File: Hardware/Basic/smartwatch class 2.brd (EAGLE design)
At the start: 38 x 38 mm, 52 parts, among them SW3 SWITCH.MOM, SW4 SWITCH.MOM, SW5 SWITCH.MOM, U1 NRF52832_MODULE_MDBT42, U4 PCF8523

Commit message: finished class 2 video
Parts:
- moved LDO2 21.6 mm to (2.64, 26.0)
- moved R12 20.8 mm to (2.11, 20.6)
- moved R11 20.7 mm to (2.57, 17.6)
- moved C20 15.5 mm to (30.4, 17.7)
- moved J2 15.2 mm to (2.18, 36.1)
- moved R14 14.4 mm to (36.2, 15.6)
- moved R13 14.2 mm to (32.4, 14.8)
- moved CHRG2 8.52 mm to (11.0, 8.79)
- moved C12 5.68 mm to (21.2, 9.42)
- moved R15 5.68 mm to (19.1, 9.37)
- moved SW3 5.08 mm to (11.4, 3.81)
- moved D5 5.08 mm to (27.1, 7.92)
- moved C21 3.81 mm to (15.5, 8.86)
- moved SW4 3.81 mm to (21.6, 3.81)
- moved C11 2.84 mm to (23.5, 9.42)
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
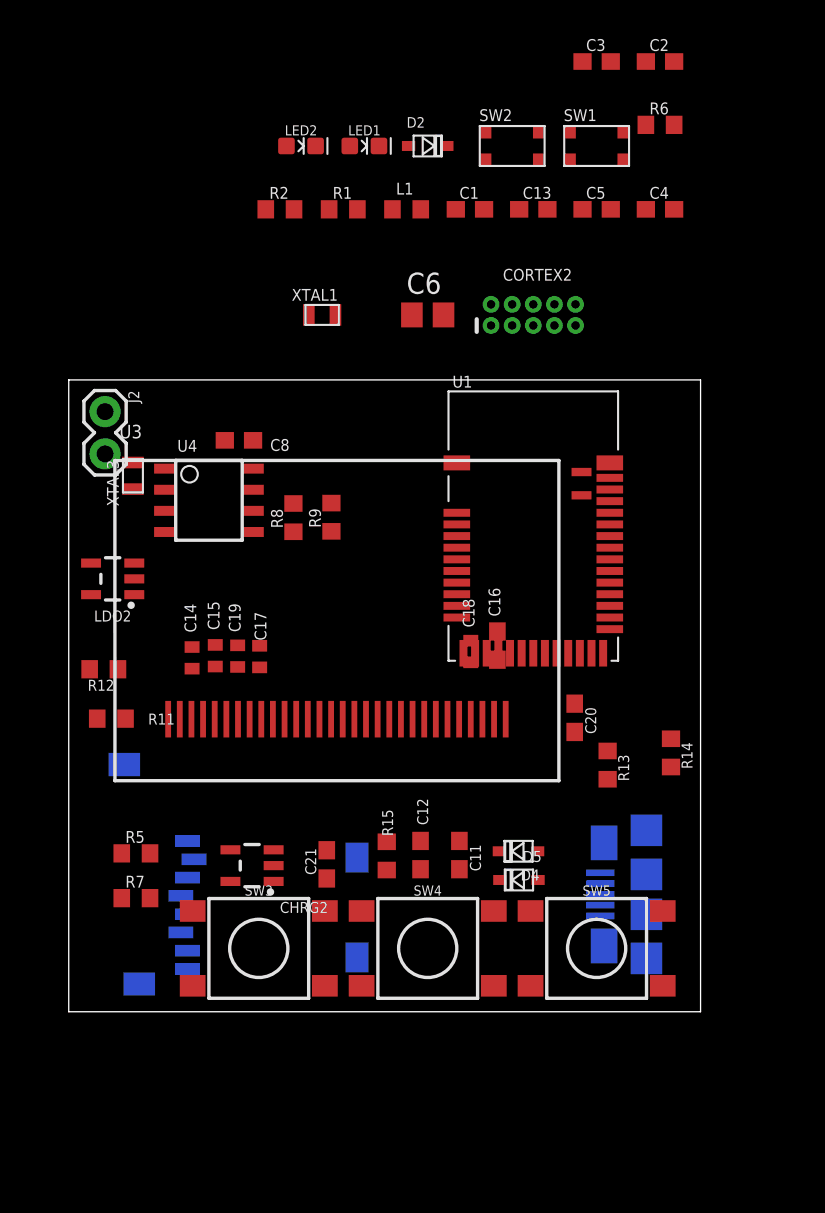
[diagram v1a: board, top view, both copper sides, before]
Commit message: deleted the second board and partially wired the board
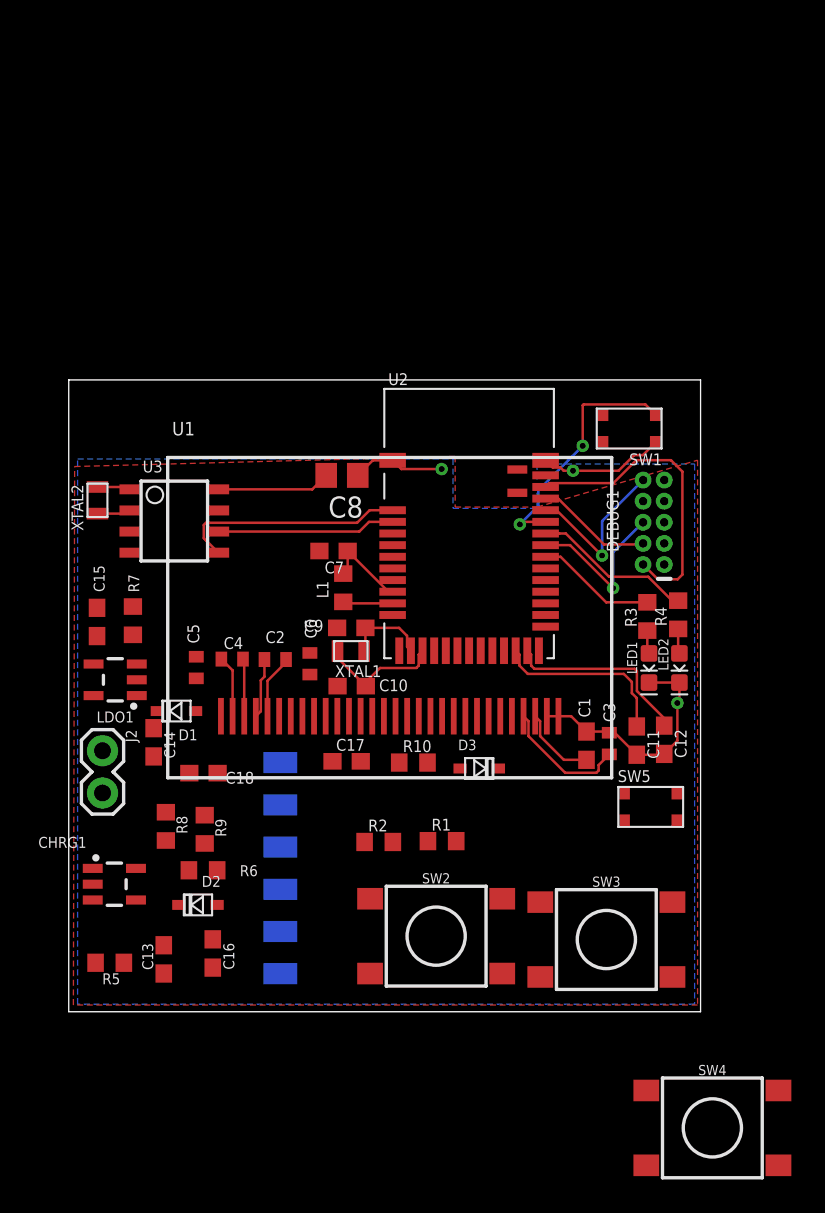
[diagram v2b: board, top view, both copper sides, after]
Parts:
- removed C19: 2.2uF, LinnesLab-Passives:C0402
- removed C20, C21: 4.7u, LinnesLab-Passives:C0603
- removed CHRG2: MCP73831, LinnesLab-Power:SOT23-5
- removed CORTEX2: CORTEX_DEBUG_PTH, LinnesLab-Connectors:2X5-PTH-1.27MM
- removed D4, D5: (no value), LinnesLab-DiscreteSemi:USC
- removed LDO2: MIC5504, LinnesLab-Power:SOT23-5
- removed R11: (no value), LinnesLab-Passives:R0603
- removed R12, R13, R14, R15: 100k, LinnesLab-Passives:R0603
- removed SD2: (no value), LinnesLab-Connectors:MICROSD
- removed U4: PCF8523, LinnesLab-Clocks:SO8
- removed USB2: USB.MICRO-BIGGERPADS, LinnesLab-Connectors:USB-MICRO-01.BIGGERPADS
- removed XTAL3: 32.7680kHz, LinnesLab-Clocks:2-SMD.NOLEAD.2.0MMTO1.2MM
- added C10, C9: (no value), LinnesLab-Passives:C0603
- added C7: 1u, LinnesLab-Passives:C0603
- added CHRG1: MCP73831, LinnesLab-Power:SOT23-5
- added D1, D3: (no value), LinnesLab-DiscreteSemi:USC
- added DEBUG1: CORTEX_DEBUG_PTH, LinnesLab-Connectors:2X5-PTH-1.27MM
- added J1: FTDI_DEVICESMD, LinnesLab-Connectors:FTDI-SMD
- added LDO1: MIC5504, LinnesLab-Power:SOT23-5
- added R10: 10k, LinnesLab-Passives:R0603
- added R3, R4: 1k, LinnesLab-Passives:R0603
- added U2: NRF52832_MODULE_MDBT42, LinnesLab-Microcontrollers:BLE_MODULE_RAYTAC_MDBT42
- added XTAL2: 32.7680kHz, LinnesLab-Clocks:2-SMD.NOLEAD.2.0MMTO1.2MM
- C1: value 1u -> 10uF
- C11, C12: value 1u -> 300p
- C13: value 100n -> 4.7u
- C14, C15, C18: value 2.2uF -> 1u; device LinnesLab-Passives:C0402 -> LinnesLab-Passives:C0603
- C16: value 10uF -> 4.7u
- C17: value 2.2uF -> 100n; device LinnesLab-Passives:C0402 -> LinnesLab-Passives:C0603
- C2, C3: value (none) -> 2.2uF; device LinnesLab-Passives:C0603 -> LinnesLab-Passives:C0402
- C4, C5: value 300p -> 2.2uF; device LinnesLab-Passives:C0603 -> LinnesLab-Passives:C0402
- C6: value 10u -> 2.2uF; device LinnesLab-Passives:C0805 -> LinnesLab-Passives:C0402
- C8: value 1u -> 10u; device LinnesLab-Passives:C0603 -> LinnesLab-Passives:C0805
- R1: value 1k -> 10k
- R2: value 1k -> 390k
- R5, R8, R9: value 10k -> 100k
- R6: value 10k -> (none)
- R7: value 390k -> 100k
- SW2: value (none) -> SWITCH.MOM; device LinnesLab-Switches:BUTTON-GULLWING -> LinnesLab-Switches:TACTILE_SWITCH_SMD_6.2MM_TALL
- SW5: value SWITCH.MOM -> (none); device LinnesLab-Switches:TACTILE_SWITCH_SMD_6.2MM_TALL -> LinnesLab-Switches:BUTTON-GULLWING
- U1: value NRF52832_MODULE_MDBT42 -> (none); device LinnesLab-Microcontrollers:BLE_MODULE_RAYTAC_MDBT42 -> LinnesLab-Displays:UG-2864HSWEG01_0.96IN_NO-WRAPAROUND
- U3: value (none) -> PCF8523; device LinnesLab-Displays:UG-2864HSWEG01_0.96IN_NO-WRAPAROUND -> LinnesLab-Clocks:SO8
- moved R6 52.6 mm to (8.08, 8.51)
- moved C13 50.3 mm to (5.71, 3.15), turned to 90 degrees
- moved SW2 47.7 mm to (22.1, 4.55)
- moved D2 47.7 mm to (7.77, 6.43), turned to 180 degrees
- moved C2 42.8 mm to (12.4, 21.2), turned to 180 degrees
- moved C3 41.0 mm to (32.5, 16.1), turned to 270 degrees
- moved LED2 38.8 mm to (36.7, 20.7), turned to 270 degrees
- moved R2 38.5 mm to (18.6, 10.2)
- moved R1 38.5 mm to (22.5, 10.3)
- moved C4 37.3 mm to (9.83, 21.2), turned to 180 degrees
- moved C5 36.6 mm to (7.67, 20.7), turned to 270 degrees
- moved LED1 35.8 mm to (34.9, 20.7), turned to 270 degrees
- moved C1 33.0 mm to (31.1, 16.0), turned to 270 degrees
- moved C16 25.2 mm to (8.66, 3.51)
- moved L1 23.1 mm to (16.5, 25.5), turned to 90 degrees
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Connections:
- removed net BATT: R13.1, R14.2
- removed net CD1: SD2.CD1
- removed net CD2: SD2.CD2
- removed net CHRG.STAT: CHRG2.1, R12.1
- removed net CS.OLED: U3.13
- removed net DC.OLED: U3.15
- removed net RESET.OLED: U3.14
- removed net SD.CS: SD2.2
- removed net USB+: USB2.3
- removed net USB-: USB2.2
- new net A4/PPG: U2.5
- new net A5/TIA: U2.6
- new net A7.BATT: R8.1, R9.2
- new net A7/BATT: U2.8
- new net D11/SW1: SW2.A1, U2.25
- new net D15/SW2: SW3.A1, U2.29
- new net D16/CS.OLED: U1.13, U2.30
- new net D27/CHRG.STAT: CHRG1.1, R5.1
- new net D27/CHRG.STATUS: U2.4
- new net D3/RESET.OLED: U1.14, U2.16
- new net D30/LED.CTRL: U2.7
- new net D4/DC.OLED: U1.15, U2.17
- new net D5/CD1: U2.18
- new net D7/SD.CS: U2.20
- new net RXD.NRF: J1.TXO
- new net TXD.NRF: J1.RXI
- net 3.3V: now also C15.1, C18.1, C5.2, C8.2, D3.-, DEBUG1.1, LDO1.5, R10.2, R7.2, U1.6, U1.9, U2.11, U3.8; no longer C12.1, C17.2, C19.2, C8.1, CORTEX2.1, D2.-, LDO2.5, R15.2, R6.2, R8.2, R9.2, SD2.4, U1.11, U3.6, U3.9, U4.8
- net DFU: now also U2.34; no longer U1.34
- net DTR: now also C17.1, J1.DTR; no longer C13.1
- net FRST: now also U2.38; no longer U1.38
- net GND: now also C1.1, C10.2, C11.2, C13.1, C14.1, C15.2, C16.2, C18.2, C3.1, C5.1, C7.2, C8.1, C9.1, CHRG1.2, DEBUG1.3, DEBUG1.5, DEBUG1.7, DEBUG1.9, J1.CTS, J1.GND, LDO1.2, R1.1, R2.2, R6.1, R7.1, R9.1, SW2.B1, SW3.B1, SW5.3, U1.10, U1.29, U1.30, U1.8, U2.1, U2.12, U2.24, U2.39, U3.4; no longer C1.2, C11.1, C16.1, C17.1, C18.1, C19.1, C2.1, C20.2, C21.1, C3.2, C4.2, C5.2, C8.2, CHRG2.2, CORTEX2.3, CORTEX2.5, CORTEX2.7, CORTEX2.9, LDO2.2, R11.1, R14.1, R15.1, R5.1, R7.2, SD2.6, SD2.MT1, SD2.MT2, SW2.3, U1.24, U1.39, U3.1, U3.10, U3.12, U3.29, U3.30, U3.8, U4.4, USB2.5
- net LED1: now also R3.2, U2.31; no longer R1.2, U1.31
- net LED2: now also R4.2, U2.33; no longer R2.2, U1.33
- net MISO: now also U2.28; no longer SD2.7, U1.28
- net MOSI: now also U1.19, U2.27; no longer SD2.3, U1.27, U3.19
- net N$1: now also C9.2, U2.13; no longer C2.2, U1.13
- net N$10: now also C4.1, U1.3; no longer C14.1, U3.3
- net N$11: now also C2.2, U1.4; no longer C15.2, U3.4
- net N$12: now also C2.1, U1.5; no longer C15.1, U3.5
- net N$13: now also DEBUG1.8; no longer CORTEX2.8
- net N$14: now also C1.2, U1.28; no longer C16.2, U3.28
- net N$15: now also C3.2, U1.27; no longer C18.2, U3.27
- net N$17: now also CHRG1.5, R6.2; no longer CHRG2.5, R11.2
- net N$19: now also U3.2, XTAL2.P$1; no longer U4.2, XTAL3.P$1
- net N$2: now also C10.1, U2.14; no longer C3.1, U1.14
- net N$20: now also U3.1, XTAL2.P$2; no longer U4.1, XTAL3.P$2
- net N$3: now also U2.10; no longer U1.10
- net N$4: now also R1.2, U1.11; no longer R5.2, U3.11
- net N$5: now also R3.1; no longer R1.1
- net N$6: now also R2.1, U1.26; no longer R7.1, U3.26
- net N$7: now also R4.1; no longer R2.1
- net N$8: now also C7.1, U2.9; no longer C1.1, U1.9
- net N$9: now also C4.2, U1.2; no longer C14.2, U3.2
- net P0.09/NFC1: now also C11.1, U2.22; no longer C5.1, U1.22
- net P0.10/NFC2: now also C12.1, U2.23; no longer C4.1, U1.23
- net RESET: now also C17.2, D3.+, DEBUG1.10, R10.1, SW5.1, U2.35; no longer C13.2, CORTEX2.10, D2.+, R6.1, SW2.1, U1.35
- net RXD: now also U2.21; no longer U1.21
- net SCK: now also U1.18, U2.26; no longer SD2.5, U1.26, U3.18
- net SCL: now also U2.3, U3.6; no longer R8.1, U1.3, U4.6
- net SDA: now also U2.2, U3.5; no longer R9.1, U1.2, U4.5
- net SWCLK: now also DEBUG1.4, U2.36; no longer CORTEX2.4, U1.36
- net SWDIO: now also DEBUG1.2, U2.37; no longer CORTEX2.2, U1.37
- net SWO: now also DEBUG1.6, U2.32; no longer CORTEX2.6, U1.32
- net TXD: now also U2.19; no longer U1.19
- net VBATT: now also U3.3; no longer U4.3
- net VIN: now also C13.2, C14.2, CHRG1.4, D1.-, D2.-, LDO1.1, LDO1.3, R5.2; no longer C11.2, C21.2, CHRG2.4, D4.-, D5.-, LDO2.1, LDO2.3, R12.2
- net VLIPO: now also C16.1, CHRG1.3, D1.+, R8.2; no longer C20.1, CHRG2.3, D4.+, R13.2
- net V_USB: now also D2.+, J1.VCC; no longer D5.+, USB2.1
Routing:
- net GND: track 0.00 -> 27.9 mm, vias 0 -> 3
- net SWDIO: track 0.00 -> 18.2 mm
- net DFU: track 0.00 -> 15.7 mm, vias 0 -> 2
- net SDA: track 0.00 -> 13.8 mm
- net P0.10/NFC2: track 0.00 -> 11.4 mm
- net P0.09/NFC1: track 0.00 -> 11.0 mm
- net SCL: track 0.00 -> 10.7 mm
- net LED2: track 0.00 -> 10.5 mm
- net RESET: track 0.00 -> 10.1 mm, vias 0 -> 1
- net SWO: track 0.00 -> 9.84 mm, vias 0 -> 1
- net N$15: track 0.00 -> 7.74 mm
- net N$2: track 0.00 -> 7.64 mm
- net LED1: track 0.00 -> 7.25 mm
- net SWCLK: track 0.00 -> 7.03 mm
- net 3.3V: track 0.00 -> 6.83 mm
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- added copper zone on layer 1, net 3.3V
- added copper zone on layer 16, net GND
